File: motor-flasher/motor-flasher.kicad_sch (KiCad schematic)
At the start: 0 parts

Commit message: Pushing current changes
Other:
- removed sheet CAN2
- removed sheet CAN3
- removed sheet CAN4

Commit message: Starting layout
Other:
- sheet LED renamed LCD
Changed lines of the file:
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@@
 			(color 0 0 0 0.0000)
 		)
-		(property "Sheetname" "LED"
+		(property "Sheetname" "LCD"
 			(at 209.55 136.4484 0)
 			(effects

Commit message: Beginning Layout Process
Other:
- sheet CAN1 ports: added CANRX, CANTX; removed none
- sheet MCU ports: added CAN_RX, CAN_TX; removed CS2, CS3, CS4, INT2, INT3, INT4, SysOff
- sheet USB + Power Source ports: added none; removed SysOff
- note removed: "Add Testpoints and LED parts for Voltage Values and Debugging"

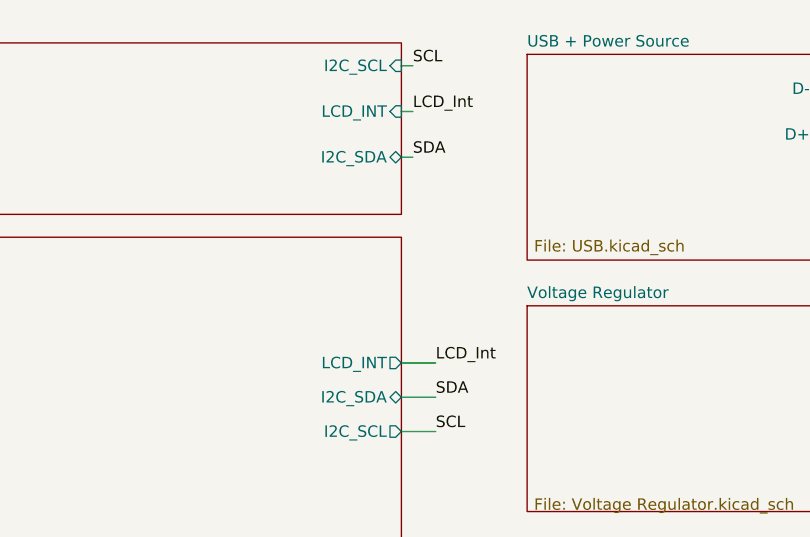
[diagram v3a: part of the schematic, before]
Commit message: Removed ERC Errors and Warnings
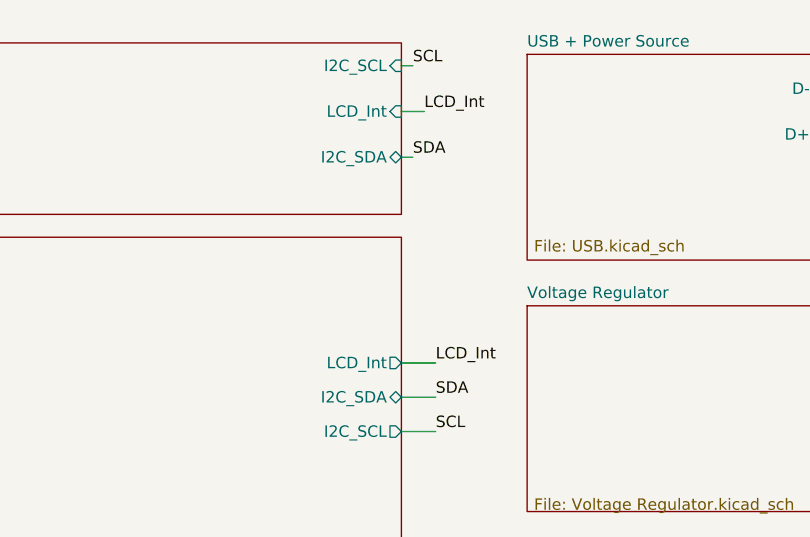
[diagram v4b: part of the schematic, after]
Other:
- sheet LCD ports: added LCD_Int; removed LCD_INT
- sheet MCU ports: added LCD_Int; removed LCD_INT
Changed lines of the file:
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@@
 	(wire
 		(pts
-			(xy 180.34 21.59) (xy 181.61 21.59)
+			(xy 180.34 21.59) (xy 182.88 21.59)
 		)
 		(stroke
@@
 	(wire
 		(pts
+			(xy 129.54 143.51) (xy 130.81 143.51)
+		)
+		(stroke
+			(width 0)
+			(type default)
+		)
+	)
+	(wire
+		(pts
+			(xy 101.6 86.36) (xy 102.87 86.36)
+		)
+		(stroke
+			(width 0)
+			(type default)
+		)
+	)
+	(wire
+		(pts
+			(xy 180.34 16.51) (xy 181.61 16.51)
+		)
+		(stroke
+			(width 0)
+			(type default)
+		)
+	)
+	(wire
+		(pts
+			(xy 100.33 67.31) (xy 102.87 67.31)
+		)
+		(stroke
+			(width 0)
+			(type default)
+		)
+	)
+	(wire
+		(pts
+			(xy 180.34 118.11) (xy 184.15 118.11)
+		)
+		(stroke
+			(width 0)
+			(type default)
+		)
+	)
+	(wire
+		(pts
 			(xy 180.34 49.53) (xy 184.15 49.53)
-		)
-		(stroke
-			(width 0)
-			(type default)
-		)
-	)
-	(wire
-		(pts
-			(xy 129.54 143.51) (xy 130.81 143.51)
-		)
-		(stroke
-			(width 0)
-			(type default)
-		)
-	)
-	(wire
-		(pts
-			(xy 101.6 86.36) (xy 102.87 86.36)
-		)
-		(stroke
-			(width 0)
-			(type default)
-		)
-	)
-	(wire
-		(pts
-			(xy 180.34 16.51) (xy 181.61 16.51)
-		)
-		(stroke
-			(width 0)
-			(type default)
-		)
-	)
-	(wire
-		(pts
-			(xy 100.33 67.31) (xy 102.87 67.31)
-		)
-		(stroke
-			(width 0)
-			(type default)
-		)
-	)
-	(wire
-		(pts
-			(xy 180.34 118.11) (xy 184.15 118.11)
 		)
 		(stroke
@@
 		)
 	)
+	(label "SDA"
+		(at 184.15 53.34 0)
+		(fields_autoplaced yes)
+		(effects
+			(font
+				(size 1.27 1.27)
+			)
+			(justify left bottom)
+		)
+	)
+	(label "SCL"
+		(at 184.15 57.15 0)
+		(fields_autoplaced yes)
+		(effects
+			(font
+				(size 1.27 1.27)
+			)
+			(justify left bottom)
+		)
+	)
+	(label "CS"
+		(at 129.54 149.86 180)
+		(fields_autoplaced yes)
+		(effects
+			(font
+				(size 1.27 1.27)
+			)
+			(justify right bottom)
+		)
+	)
+	(label "CANTX"
+		(at 158.75 149.86 0)
+		(fields_autoplaced yes)
+		(effects
+			(font
+				(size 1.27 1.27)
+			)
+			(justify left bottom)
+		)
+	)
+	(label "LCD_Int"
+		(at 182.88 21.59 0)
+		(fields_autoplaced yes)
+		(effects
+			(font
+				(size 1.27 1.27)
+			)
+			(justify left bottom)
+		)
+	)
+	(label "Deb_select"
+		(at 184.15 114.3 0)
+		(fields_autoplaced yes)
+		(effects
+			(font
+				(size 1.27 1.27)
+			)
+			(justify left bottom)
+		)
+	)
+	(label "D-"
+		(at 101.6 86.36 180)
+		(fields_autoplaced yes)
+		(effects
+			(font
+				(size 1.27 1.27)
+			)
+			(justify right bottom)
+		)
+	)
+	(label "INT"
+		(at 100.33 74.93 180)
+		(fields_autoplaced yes)
+		(effects
+			(font
+				(size 1.27 1.27)
+			)
+			(justify right bottom)
+		)
+	)
+	(label "SCK"
+		(at 100.33 69.85 180)
+		(fields_autoplaced yes)
+		(effects
+			(font
+				(size 1.27 1.27)
+			)
+			(justify right bottom)
+		)
+	)
+	(label "Deb_select"
+		(at 184.15 87.63 0)
+		(fields_autoplaced yes)
+		(effects
+			(font
+				(size 1.27 1.27)
+			)
+			(justify left bottom)
+		)
+	)
+	(label "Deb_Up"
+		(at 184.15 83.82 0)
+		(fields_autoplaced yes)
+		(effects
+			(font
+				(size 1.27 1.27)
+			)
+			(justify left bottom)
+		)
+	)
+	(label "Deb_back"
+		(at 184.15 91.44 0)
+		(fields_autoplaced yes)
+		(effects
+			(font
+				(size 1.27 1.27)
+			)
+			(justify left bottom)
+		)
+	)
+	(label "CANRX"
+		(at 100.33 55.88 180)
+		(fields_autoplaced yes)
+		(effects
+			(font
+				(size 1.27 1.27)
+			)
+			(justify right bottom)
+		)
+	)
+	(label "CANRX"
+		(at 158.75 146.05 0)
+		(fields_autoplaced yes)
+		(effects
+			(font
+				(size 1.27 1.27)
+			)
+			(justify left bottom)
+		)
+	)
+	(label "D+"
+		(at 228.6 24.13 0)
+		(fields_autoplaced yes)
+		(effects
+			(font
+				(size 1.27 1.27)
+			)
+			(justify left bottom)
+		)
+	)
 	(label "LCD_Int"
 		(at 184.15 49.53 0)
-		(fields_autoplaced yes)
-		(effects
-			(font
-				(size 1.27 1.27)
-			)
-			(justify left bottom)
-		)
-	)
-	(label "SDA"
-		(at 184.15 53.34 0)
-		(fields_autoplaced yes)
-		(effects
-			(font
-				(size 1.27 1.27)
-			)
-			(justify left bottom)
-		)
-	)
-	(label "SCL"
-		(at 184.15 57.15 0)
-		(fields_autoplaced yes)
-		(effects
-			(font
-				(size 1.27 1.27)
-			)
-			(justify left bottom)
-		)
-	)
-	(label "LCD_Int"
-		(at 181.61 21.59 0)
-		(fields_autoplaced yes)
-		(effects
-			(font
-				(size 1.27 1.27)
-			)
-			(justify left bottom)
-		)
-	)
-	(label "CS"
-		(at 129.54 149.86 180)
-		(fields_autoplaced yes)
-		(effects
-			(font
-				(size 1.27 1.27)
-			)
-			(justify right bottom)
-		)
-	)
-	(label "CANTX"
-		(at 158.75 149.86 0)
-		(fields_autoplaced yes)
-		(effects
-			(font
-				(size 1.27 1.27)
-			)
-			(justify left bottom)
-		)
-	)
-	(label "Deb_select"
-		(at 184.15 114.3 0)
-		(fields_autoplaced yes)
-		(effects
-			(font
-				(size 1.27 1.27)
-			)
-			(justify left bottom)
-		)
-	)
-	(label "D-"
-		(at 101.6 86.36 180)
-		(fields_autoplaced yes)
-		(effects
-			(font
-				(size 1.27 1.27)
-			)
-			(justify right bottom)
-		)
-	)
-	(label "INT"
-		(at 100.33 74.93 180)
-		(fields_autoplaced yes)
-		(effects
-			(font
-				(size 1.27 1.27)
-			)
-			(justify right bottom)
-		)
-	)
-	(label "SCK"
-		(at 100.33 69.85 180)
-		(fields_autoplaced yes)
-		(effects
-			(font
-				(size 1.27 1.27)
-			)
-			(justify right bottom)
-		)
-	)
-	(label "Deb_select"
-		(at 184.15 87.63 0)
-		(fields_autoplaced yes)
-		(effects
-			(font
-				(size 1.27 1.27)
-			)
-			(justify left bottom)
-		)
-	)
-	(label "Deb_Up"
-		(at 184.15 83.82 0)
-		(fields_autoplaced yes)
-		(effects
-			(font
-				(size 1.27 1.27)
-			)
-			(justify left bottom)
-		)
-	)
-	(label "Deb_back"
-		(at 184.15 91.44 0)
-		(fields_autoplaced yes)
-		(effects
-			(font
-				(size 1.27 1.27)
-			)
-			(justify left bottom)
-		)
-	)
-	(label "CANRX"
-		(at 100.33 55.88 180)
-		(fields_autoplaced yes)
-		(effects
-			(font
-				(size 1.27 1.27)
-			)
-			(justify right bottom)
-		)
-	)
-	(label "CANRX"
-		(at 158.75 146.05 0)
-		(fields_autoplaced yes)
-		(effects
-			(font
-				(size 1.27 1.27)
-			)
-			(justify left bottom)
-		)
-	)
-	(label "D+"
-		(at 228.6 24.13 0)
 		(fields_autoplaced yes)
 		(effects
@@
 			)
 		)
-		(pin "LCD_INT" input
-			(at 180.34 21.59 0)
-			(effects
-				(font
-					(size 1.27 1.27)
-				)
-				(justify right)
-			)
-		)
 		(pin "I2C_SDA" bidirectional
 			(at 180.34 26.67 0)
+			(effects
+				(font
+					(size 1.27 1.27)
+				)
+				(justify right)
+			)
+		)
+		(pin "LCD_Int" input
+			(at 180.34 21.59 0)
 			(effects
 				(font
@@
 			)
 		)
-		(pin "LCD_INT" output
-			(at 180.34 49.53 0)
-			(effects
-				(font
-					(size 1.27 1.27)
-				)
-				(justify right)
-			)
-		)
 		(pin "I2C_SCL" output
 			(at 180.34 57.15 0)
@@
 			)
 		)
+		(pin "LCD_Int" output
+			(at 180.34 49.53 0)
+			(effects
+				(font
+					(size 1.27 1.27)
+				)
+				(justify right)
+			)
+		)
